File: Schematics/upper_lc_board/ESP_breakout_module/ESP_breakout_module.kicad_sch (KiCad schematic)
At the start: 20 parts, among them U1 ESP32-S3-WROOM-1-N16R2, U3 PD_D3V3XA4B10LP, U4 CAN_T_SN65HVD230DR

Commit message: start solenoid driver circuitry
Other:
- title: ESP32-S3 Breakout Circuitry -> ULC Board ESP32-S3 Breakout Circuitry 
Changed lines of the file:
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@@
 	(paper "A4")
 	(title_block
-		(title "ESP32-S3 Breakout Circuitry")
+		(title "ULC Board ESP32-S3 Breakout Circuitry ")
 		(rev "A")
 		(company "Queen's Rocket Engineering Team")

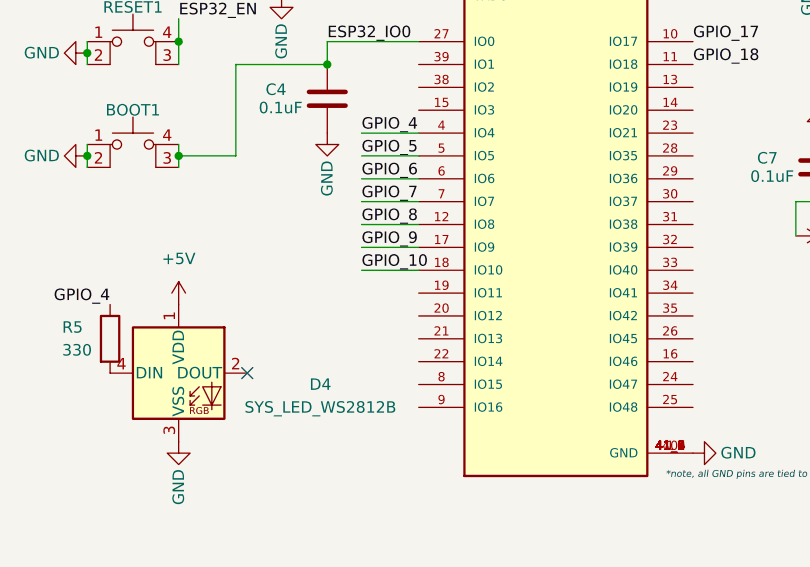
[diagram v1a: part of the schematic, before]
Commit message: add solenoid driver circuitry
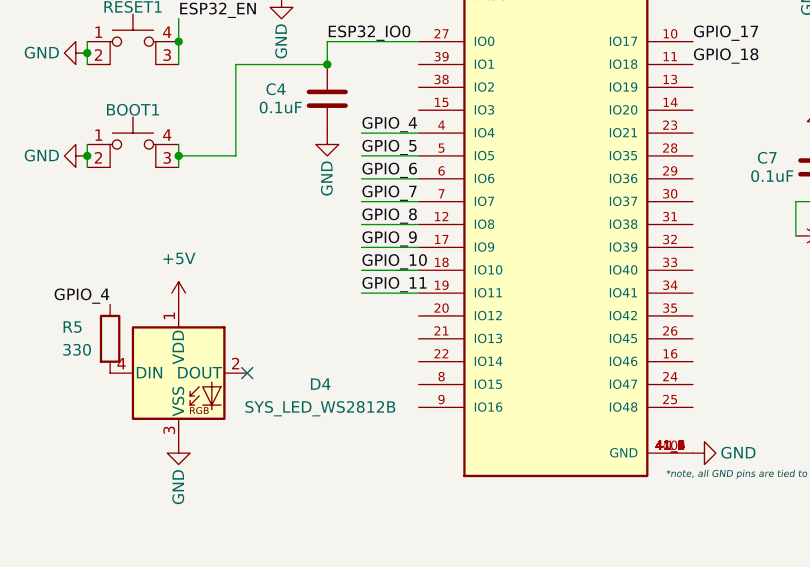
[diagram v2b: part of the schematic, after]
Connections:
- net GPIO_11: now reaches U1.19 (IO11)
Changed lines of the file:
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@@
+	(wire
+		(pts
+			(xy 93.98 102.87) (xy 100.33 102.87)
+		)
+		(stroke
+			(width 0)
+			(type default)
+		)
+	)
 	(wire
 		(pts
@@
 		(fields_autoplaced yes)
 		(effects
+			(font
+				(size 1.27 1.27)
+			)
+			(justify left bottom)
+		)
+	)
+	(label "GPIO_11"
+		(at 93.98 102.87 0)
+		(fields_autoplaced yes)
+		(effects

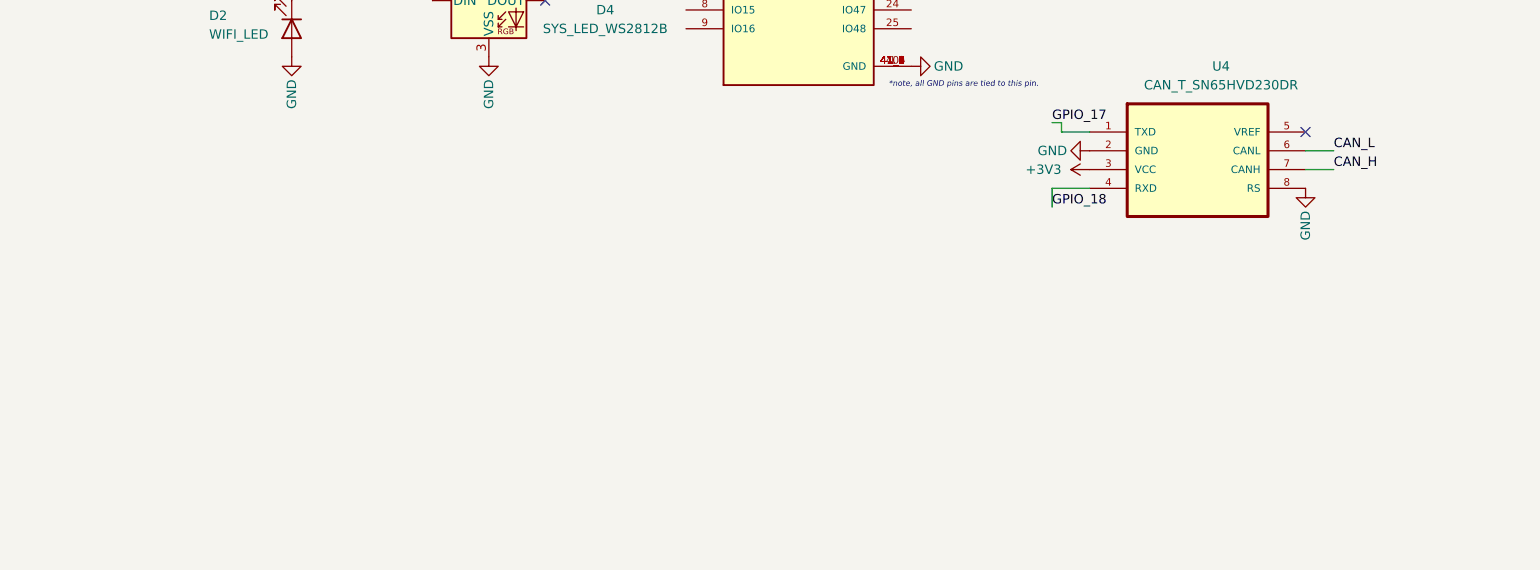
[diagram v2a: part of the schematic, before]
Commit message: SSR replacement for solenoid driver
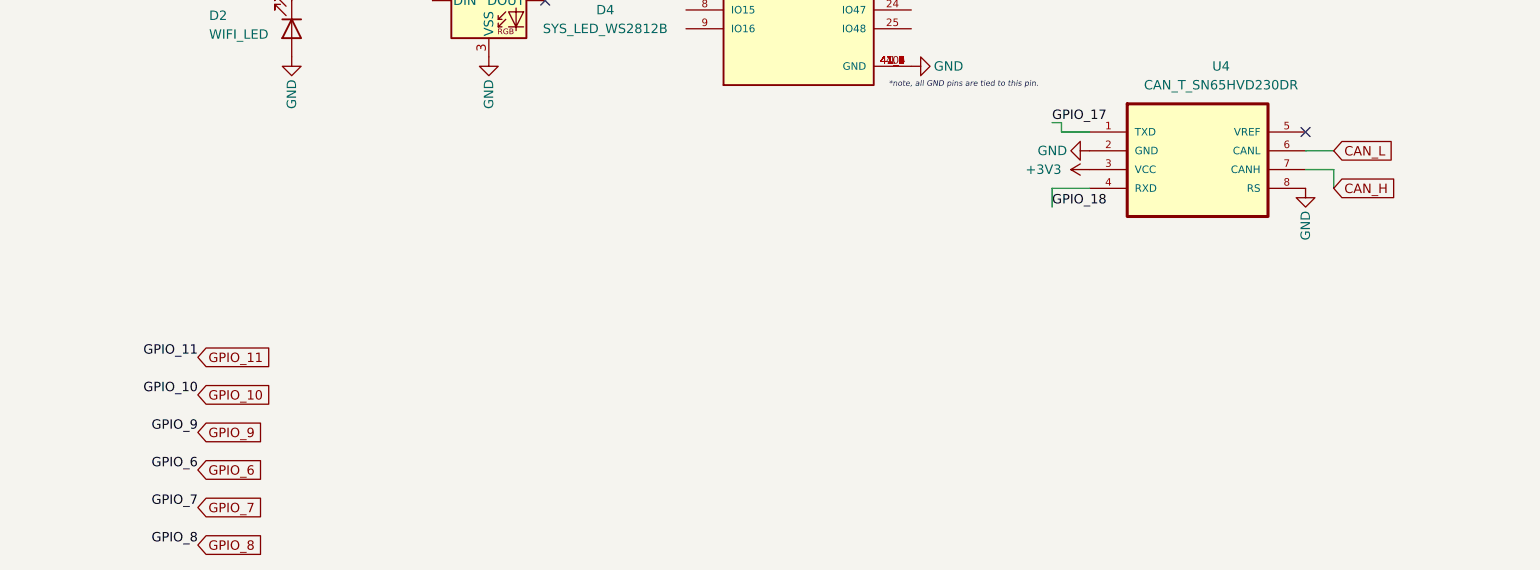
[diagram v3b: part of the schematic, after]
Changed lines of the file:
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@@
+	(wire
+		(pts
+			(xy 187.96 134.62) (xy 187.96 137.16)
+		)
+		(stroke
+			(width 0)
+			(type default)
+		)
+	)
 	(wire
 		(pts
@@
 		)
 	)
+	(label "GPIO_6"
+		(at 34.29 175.26 180)
+		(fields_autoplaced yes)
+		(effects
+			(font
+				(size 1.27 1.27)
+			)
+			(justify right bottom)
+		)
+	)
 	(label "GPIO_8"
 		(at 93.98 95.25 0)
@@
 		)
 	)
+	(label "GPIO_7"
+		(at 34.29 180.34 180)
+		(fields_autoplaced yes)
+		(effects
+			(font
+				(size 1.27 1.27)
+			)
+			(justify right bottom)
+		)
+	)
+	(label "GPIO_9"
+		(at 34.29 170.18 180)
+		(fields_autoplaced yes)
+		(effects
+			(font
+				(size 1.27 1.27)
+			)
+			(justify right bottom)
+		)
+	)
 	(label "GPIO_11"
 		(at 93.98 102.87 0)
@@
 		)
 	)
-	(label "CAN_L"
-		(at 187.96 132.08 0)
-		(fields_autoplaced yes)
-		(effects
-			(font
-				(size 1.27 1.27)
-			)
-			(justify left bottom)
-		)
-	)
 	(label "ESP32_EN"
 		(at 91.44 62.23 0)
@@
 		)
 	)
+	(label "GPIO_11"
+		(at 34.29 160.02 180)
+		(fields_autoplaced yes)
+		(effects
+			(font
+				(size 1.27 1.27)
+			)
+			(justify right bottom)
+		)
+	)
 	(label "GPIO_17"
 		(at 149.86 128.27 0)
@@
 		)
 	)
-	(label "CAN_H"
-		(at 187.96 134.62 0)
-		(fields_autoplaced yes)
-		(effects
-			(font
-				(size 1.27 1.27)
-			)
-			(justify left bottom)
+	(label "GPIO_10"
+		(at 34.29 165.1 180)
+		(fields_autoplaced yes)
+		(effects
+			(font
+				(size 1.27 1.27)
+			)
+			(justify right bottom)
+		)
+	)
+	(label "GPIO_8"
+		(at 34.29 185.42 180)
+		(fields_autoplaced yes)
+		(effects
+			(font
+				(size 1.27 1.27)
+			)
+			(justify right bottom)
 		)
 	)
@@
 		)
 	)
+	(global_label "GPIO_7"
+		(shape input)
+		(at 34.29 180.34 0)
+		(fields_autoplaced yes)
+		(effects
+			(font
+				(size 1.27 1.27)
+			)
+			(justify left)
+		)
+		(property "Intersheetrefs" "${INTERSHEET_REFS}"
+			(at 43.9276 180.34 0)
+			(effects
+				(font
+					(size 1.27 1.27)
+				)
+				(justify left)
+				(hide yes)
+			)
+		)
+	)
+	(global_label "GPIO_6"
+		(shape input)
+		(at 34.29 175.26 0)
+		(fields_autoplaced yes)
+		(effects
+			(font
+				(size 1.27 1.27)
+			)
+			(justify left)
+		)
+		(property "Intersheetrefs" "${INTERSHEET_REFS}"
+			(at 43.9276 175.26 0)
+			(effects
+				(font
+					(size 1.27 1.27)
+				)
+				(justify left)
+				(hide yes)
+			)
+		)
+	)
+	(global_label "GPIO_10"
+		(shape input)
+		(at 34.29 165.1 0)
+		(fields_autoplaced yes)
+		(effects
+			(font
+				(size 1.27 1.27)
+			)
+			(justify left)
+		)
+		(property "Intersheetrefs" "${INTERSHEET_REFS}"
+			(at 45.1371 165.1 0)
+			(effects
+				(font
+					(size 1.27 1.27)
+				)
+				(justify left)
+				(hide yes)
+			)
+		)
+	)
+	(global_label "GPIO_8"
+		(shape input)
+		(at 34.29 185.42 0)
+		(fields_autoplaced yes)
+		(effects
+			(font
+				(size 1.27 1.27)
+			)
+			(justify left)
+		)
+		(property "Intersheetrefs" "${INTERSHEET_REFS}"
+			(at 43.9276 185.42 0)
+			(effects
+				(font
+					(size 1.27 1.27)
+				)
+				(justify left)
+				(hide yes)
+			)
+		)
+	)
+	(global_label "GPIO_9"
+		(shape input)
+		(at 34.29 170.18 0)
+		(fields_autoplaced yes)
+		(effects
+			(font
+				(size 1.27 1.27)
+			)
+			(justify left)
+		)
+		(property "Intersheetrefs" "${INTERSHEET_REFS}"
+			(at 43.9276 170.18 0)
+			(effects
+				(font
+					(size 1.27 1.27)
+				)
+				(justify left)
+				(hide yes)
+			)
+		)
+	)
+	(global_label "CAN_H"
+		(shape input)
+		(at 187.96 137.16 0)
+		(fields_autoplaced yes)
+		(effects
+			(font
+				(size 1.27 1.27)
+			)
+			(justify left)
+		)
+		(property "Intersheetrefs" "${INTERSHEET_REFS}"
+			(at 196.9324 137.16 0)
+			(effects
+				(font
+					(size 1.27 1.27)
+				)
+				(justify left)
+				(hide yes)
+			)
+		)
+	)
+	(global_label "CAN_L"
+		(shape input)
+		(at 187.96 132.08 0)
+		(fields_autoplaced yes)
+		(effects
+			(font
+				(size 1.27 1.27)
+			)
+			(justify left)
+		)
+		(property "Intersheetrefs" "${INTERSHEET_REFS}"
+			(at 196.63 132.08 0)
+			(effects
+				(font
+					(size 1.27 1.27)
+				)
+				(justify left)
+				(hide yes)
+			)
+		)
+	)
+	(global_label "GPIO_11"
+		(shape input)
+		(at 34.29 160.02 0)
+		(fields_autoplaced yes)
+		(effects
+			(font
+				(size 1.27 1.27)
+			)
+			(justify left)
+		)
+		(property "Intersheetrefs" "${INTERSHEET_REFS}"
+			(at 45.1371 160.02 0)
+			(effects
+				(font
+					(size 1.27 1.27)
+				)
+				(justify left)
+				(hide yes)
+			)
+		)
+	)

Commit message: add hiearchical sheets in main board file
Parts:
- renumbered BOOT1 to BOOT2, C2 to C10, C3 to C5, C4 to C6, C7 to C9, D2 to D1, D4 to D3, JUSB1 to JUSB2, R2 to R12, R9 to R13, R10 to R14, R4 to R6, R5 to R7, R3 to R8, RESET1 to RESET2

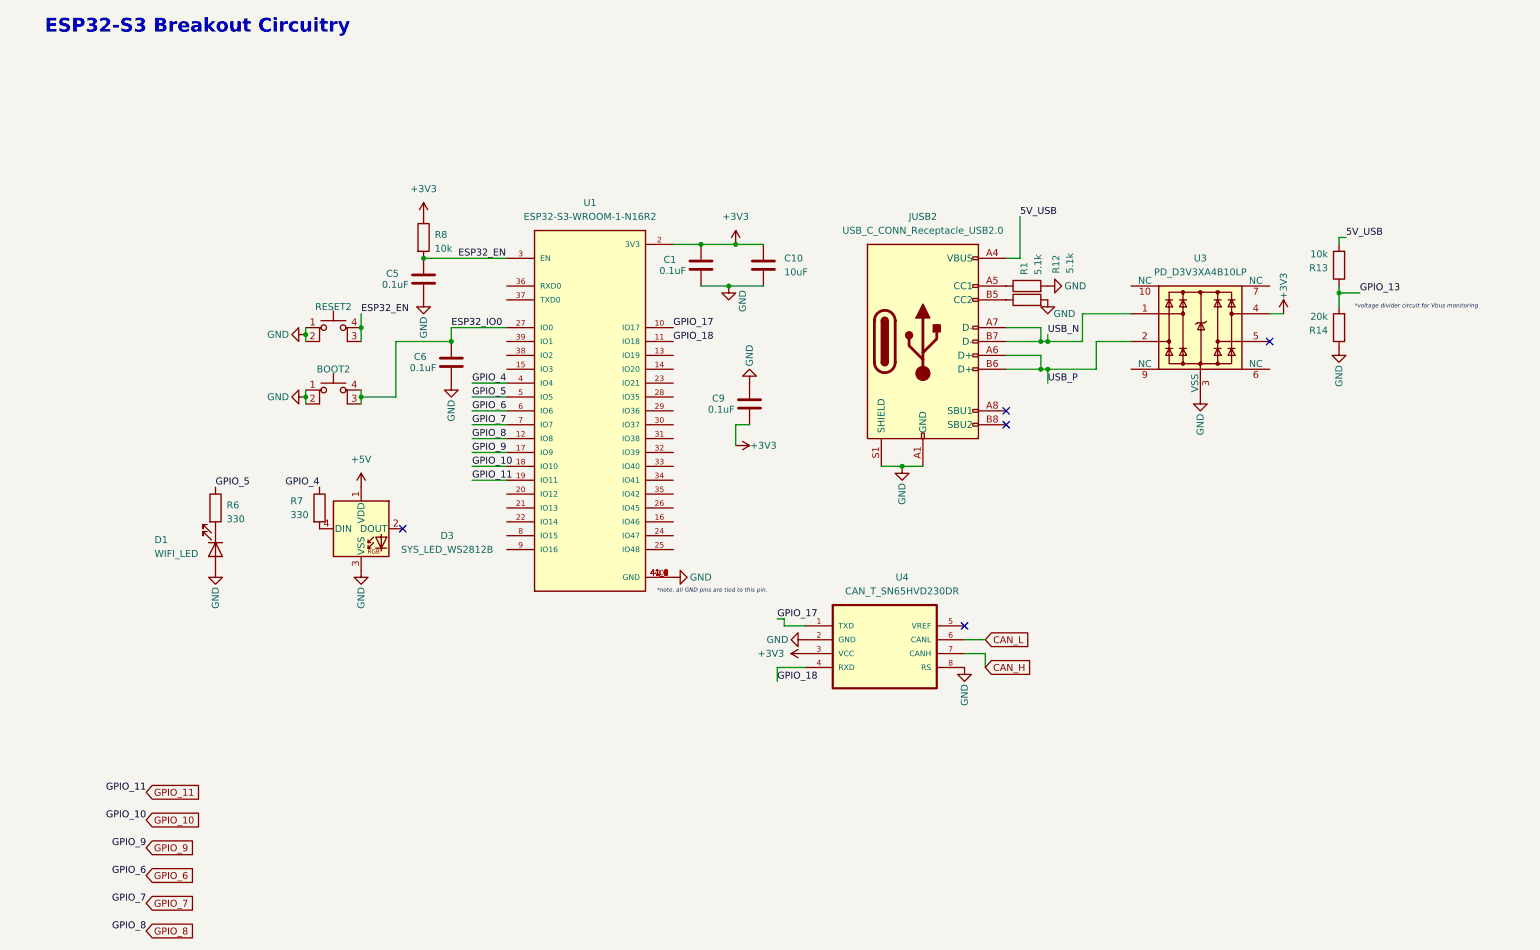
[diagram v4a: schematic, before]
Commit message: global symbols/component annotations fix
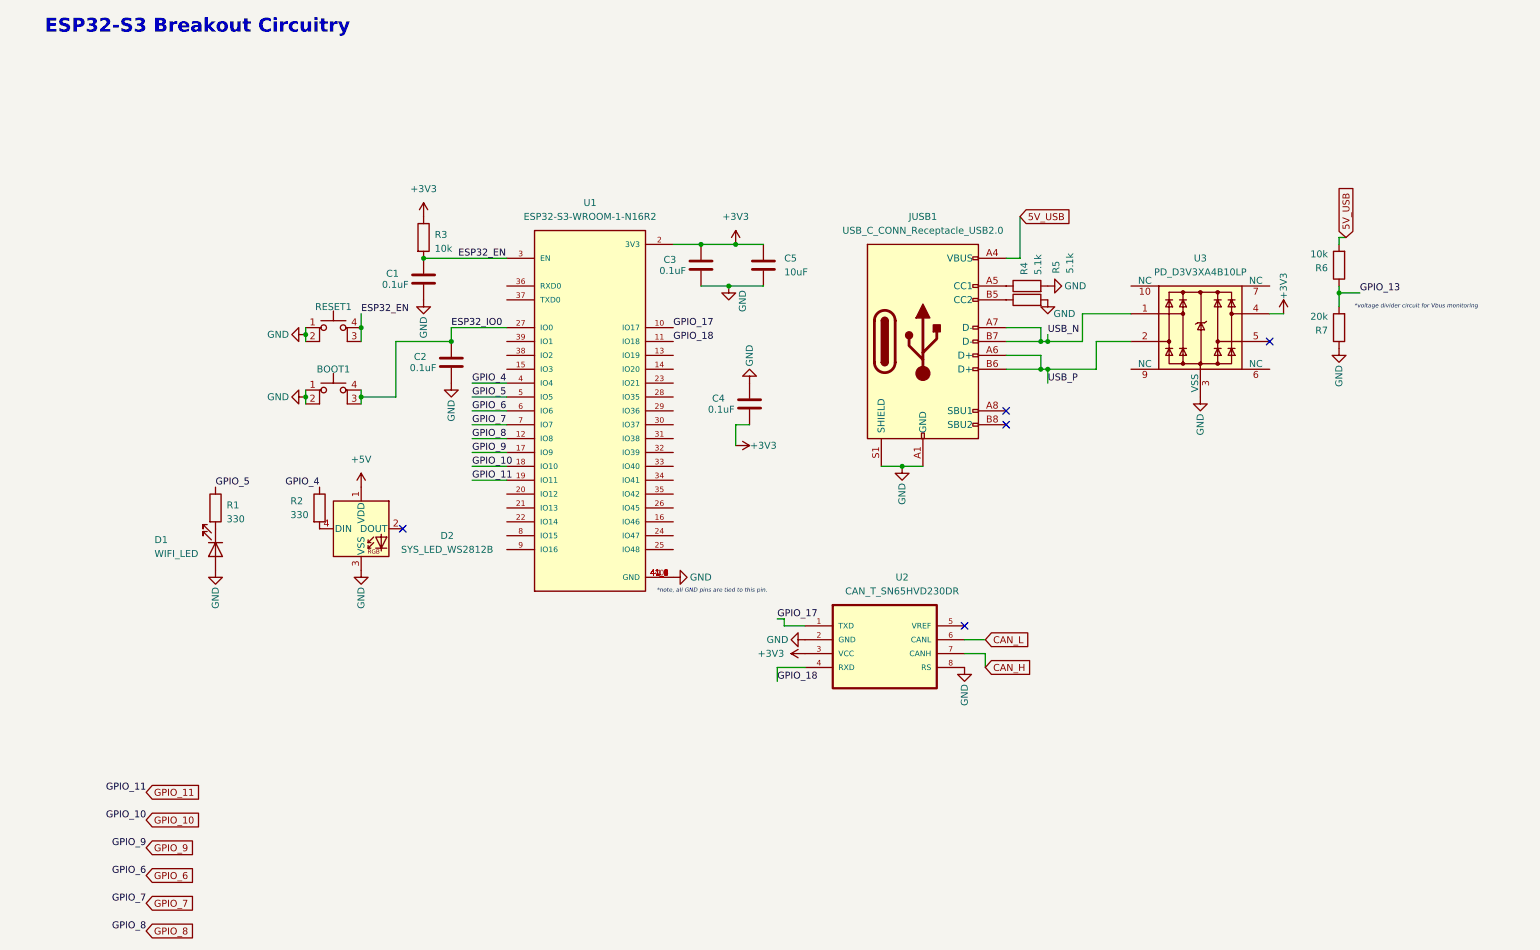
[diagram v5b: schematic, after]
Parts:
- renumbered BOOT2 to BOOT1, C5 to C1, C6 to C2, C1 to C3, C9 to C4, C10 to C5, D3 to D2, JUSB2 to JUSB1, R6 to R1, R7 to R2, R8 to R3, R1 to R4, R12 to R5, R13 to R6, R14 to R7, RESET2 to RESET1, U4 to U2

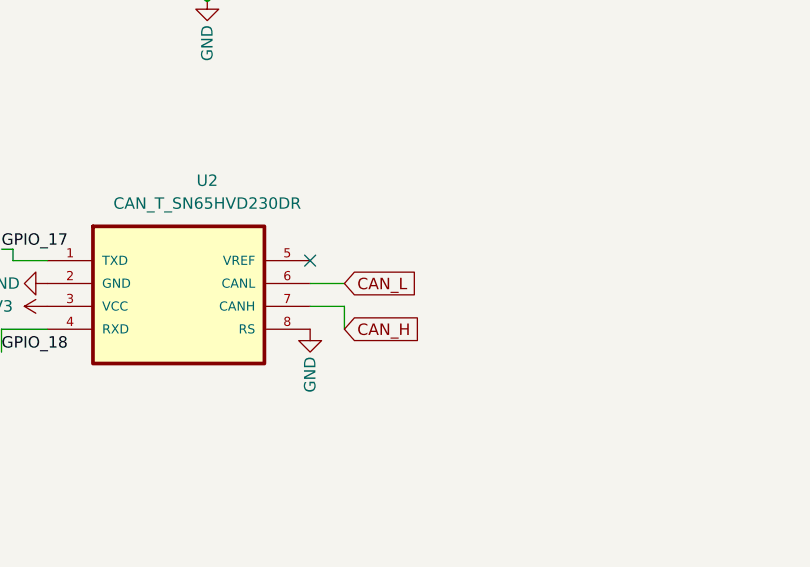
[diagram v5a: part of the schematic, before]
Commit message: start PCB file, start assigning footprints, omit fuse, JST conns for now, still assigning resistors and some diodes
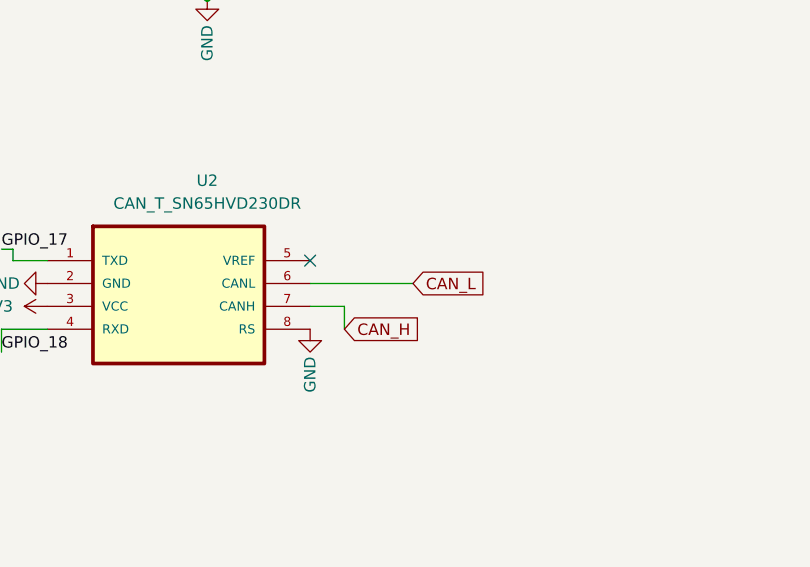
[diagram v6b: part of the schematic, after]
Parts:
- BOOT1, RESET1: footprint Button_Switch_SMD:SW_SPST_PTS810 -> Button_Switch_SMD:SW_Push_1P1T_XKB_TS-1187A
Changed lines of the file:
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@@
 	(wire
 		(pts
-			(xy 184.15 132.08) (xy 187.96 132.08)
+			(xy 184.15 132.08) (xy 195.58 132.08)
 		)
 		(stroke
@@
 		)
 	)
+	(global_label "CAN_L"
+		(shape input)
+		(at 195.58 132.08 0)
+		(fields_autoplaced yes)
+		(effects
+			(font
+				(size 1.27 1.27)
+			)
+			(justify left)
+		)
+		(property "Intersheetrefs" "${INTERSHEET_REFS}"
+			(at 204.25 132.08 0)
+			(effects
+				(font
+					(size 1.27 1.27)
+				)
+				(justify left)
+				(hide yes)
+			)
+		)
+	)
+	(global_label "CAN_H"
+		(shape input)
+		(at 187.96 137.16 0)
+		(fields_autoplaced yes)
+		(effects
+			(font
+				(size 1.27 1.27)
+			)
+			(justify left)
+		)
+		(property "Intersheetrefs" "${INTERSHEET_REFS}"
+			(at 196.9324 137.16 0)
+			(effects
+				(font
+					(size 1.27 1.27)
+				)
+				(justify left)
+				(hide yes)
+			)
+		)
+	)
 	(global_label "GPIO_9"
 		(shape input)
@@
 		(property "Intersheetrefs" "${INTERSHEET_REFS}"
 			(at 43.9276 170.18 0)
-			(effects
-				(font
-					(size 1.27 1.27)
-				)
-				(justify left)
-				(hide yes)
-			)
-		)
-	)
-	(global_label "CAN_H"
-		(shape input)
-		(at 187.96 137.16 0)
-		(fields_autoplaced yes)
-		(effects
-			(font
-				(size 1.27 1.27)
-			)
-			(justify left)
-		)
-		(property "Intersheetrefs" "${INTERSHEET_REFS}"
-			(at 196.9324 137.16 0)
-			(effects
-				(font
-					(size 1.27 1.27)
-				)
-				(justify left)
-				(hide yes)
-			)
-		)
-	)
-	(global_label "CAN_L"
-		(shape input)
-		(at 187.96 132.08 0)
-		(fields_autoplaced yes)
-		(effects
-			(font
-				(size 1.27 1.27)
-			)
-			(justify left)
-		)
-		(property "Intersheetrefs" "${INTERSHEET_REFS}"
-			(at 196.63 132.08 0)
 			(effects
 				(font
@@
 			)
 		)
-		(property "Footprint" "Button_Switch_SMD:SW_SPST_PTS810"
+		(property "Footprint" "Button_Switch_SMD:SW_Push_1P1T_XKB_TS-1187A"
 			(at 68.58 81.28 0)
 			(effects
@@
 			)
 		)
-		(property "Footprint" "Button_Switch_SMD:SW_SPST_PTS810"
+		(property "Footprint" "Button_Switch_SMD:SW_Push_1P1T_XKB_TS-1187A"
 			(at 68.58 69.85 0)
 			(effects

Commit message: layout update; still need to add small components (caps, resistors), and add silkscreen
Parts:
- R1, R2, R3, R4, R5, R6, R7: footprint Resistor_SMD:R_0603_1608Metric -> Capacitor_SMD:C_0402_1005Metric
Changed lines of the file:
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@@
 			)
 		)
-		(property "Footprint" "Resistor_SMD:R_0603_1608Metric"
+		(property "Footprint" "Capacitor_SMD:C_0402_1005Metric"
 			(at 254.508 74.93 90)
 			(effects
@@
 			)
 		)
-		(property "Footprint" "Resistor_SMD:R_0603_1608Metric"
+		(property "Footprint" "Capacitor_SMD:C_0402_1005Metric"
 			(at 64.262 107.95 90)
 			(effects
@@
 			)
 		)
-		(property "Footprint" "Resistor_SMD:R_0603_1608Metric"
+		(property "Footprint" "Capacitor_SMD:C_0402_1005Metric"
 			(at 254.508 63.5 90)
 			(effects
@@
 			)
 		)
-		(property "Footprint" "Resistor_SMD:R_0603_1608Metric"
+		(property "Footprint" "Capacitor_SMD:C_0402_1005Metric"
 			(at 45.212 107.95 90)
 			(effects
@@
 			)
 		)
-		(property "Footprint" "Resistor_SMD:R_0603_1608Metric"
+		(property "Footprint" "Capacitor_SMD:C_0402_1005Metric"
 			(at 83.312 58.42 90)
 			(effects
@@
 			)
 		)
-		(property "Footprint" "Resistor_SMD:R_0603_1608Metric"
+		(property "Footprint" "Capacitor_SMD:C_0402_1005Metric"
 			(at 195.58 69.088 90)
 			(effects
@@
 			)
 		)
-		(property "Footprint" "Resistor_SMD:R_0603_1608Metric"
+		(property "Footprint" "Capacitor_SMD:C_0402_1005Metric"
 			(at 195.58 71.628 90)
 			(effects
